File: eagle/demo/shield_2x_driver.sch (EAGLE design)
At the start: 19 parts, among them X1 MALE_2X1-T-VERTICAL, X2 MALE_2X1-T-VERTICAL, X301 MALE_2X1-T-VERTICAL, X302 MALE_2X10-T-VERTICAL_2.54MM

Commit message: fix partcodes
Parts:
- LED301: value (none) -> green; FUNCTION (none) -> DRV 1 ON; PART_CODE_BEL (none) -> LED_PAC_S_0805_VAL_green
- LED401: value (none) -> green; FUNCTION (none) -> DRV 2 ON; PART_CODE_BEL (none) -> LED_PAC_S_0805_VAL_green
- LED501: value (none) -> red; FUNCTION (none) -> BUTTON PRESSED; PART_CODE_BEL (none) -> LED_PAC_S_0805_VAL_red
- R301, R401, R501: PART_CODE_BEL (none) -> R_PAC_S_0805_VAL_330
- X101: PART_CODE_BEL (none) -> X_PAC_T_MALE_2X10_VERTICAL_PITCH_2mm54
- renumbered FD1 to FD101, FD2 to FD102, H1 to H103, H2 to H104, H3 to H101, H4 to H102, LED1 to LED401, LED3 to LED501, LED4 to LED301, N1 to N202, N2 to N203, N3 to N201, R1 to R401, R3 to R501, R4 to R301, X1 to X501, X2 to X401, X302 to X101

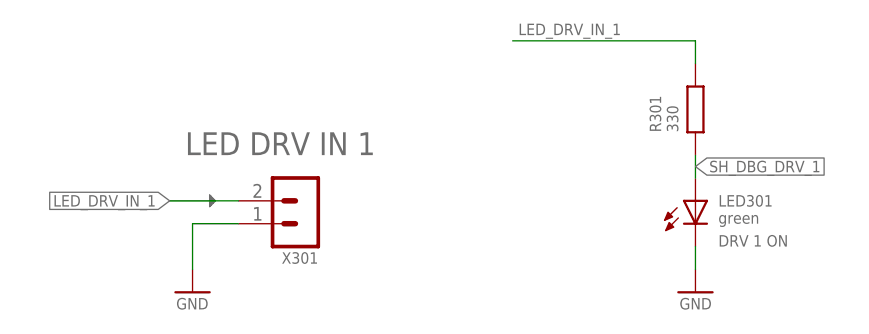
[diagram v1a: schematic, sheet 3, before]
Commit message: fix net names
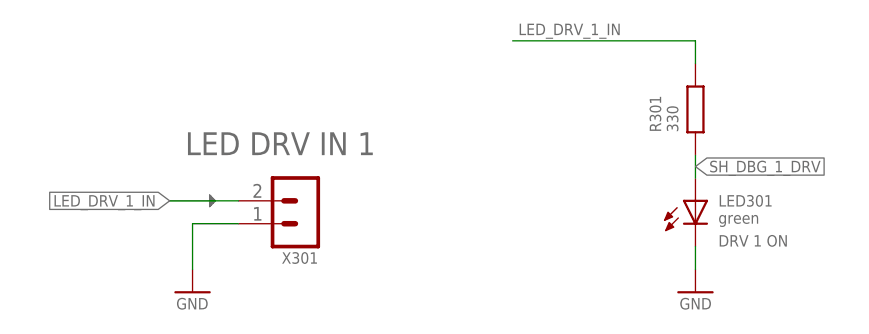
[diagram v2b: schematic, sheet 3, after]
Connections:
- net LED_DRV_IN_1 renamed LED_DRV_1_IN
- net LED_DRV_IN_2 renamed LED_DRV_2_IN
- net SH_DBG_DRV_1 renamed SH_DBG_1_DRV
- net SH_DBG_DRV_2 renamed SH_DBG_2_DRV
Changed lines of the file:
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@@
 </segment>
 </net>
-<net name="LED_DRV_IN_1" class="0">
+<net name="LED_DRV_1_IN" class="0">
 <segment>
 <pinref part="N202" gate="G$1" pin="1"/>
@@
 </segment>
 </net>
-<net name="LED_DRV_IN_2" class="0">
+<net name="LED_DRV_2_IN" class="0">
 <segment>
 <pinref part="N201" gate="G$1" pin="1"/>
@@
 </segment>
 </net>
-<net name="LED_DRV_IN_1" class="0">
+<net name="LED_DRV_1_IN" class="0">
 <segment>
 <pinref part="R301" gate="G$1" pin="2"/>
@@
 </segment>
 </net>
-<net name="SH_DBG_DRV_1" class="0">
+<net name="SH_DBG_1_DRV" class="0">
 <segment>
 <pinref part="R301" gate="G$1" pin="1"/>
@@
 </segment>
 </net>
-<net name="LED_DRV_IN_2" class="0">
+<net name="LED_DRV_2_IN" class="0">
 <segment>
 <pinref part="R401" gate="G$1" pin="2"/>
@@
 </segment>
 </net>
-<net name="SH_DBG_DRV_2" class="0">
+<net name="SH_DBG_2_DRV" class="0">
 <segment>
 <pinref part="R401" gate="G$1" pin="1"/>
